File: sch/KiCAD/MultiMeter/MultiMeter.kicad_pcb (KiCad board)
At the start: 2 copper layers, 35.6 x 52.7 mm, 20 parts, among them J1 Conn_01x02_Male, J2 Conn_01x02_Male, J3 Conn_01x03_Male, J4 Conn_01x03_Male, J5 Conn_01x02_Female, J6 Conn_01x15, J7 Conn_01x15

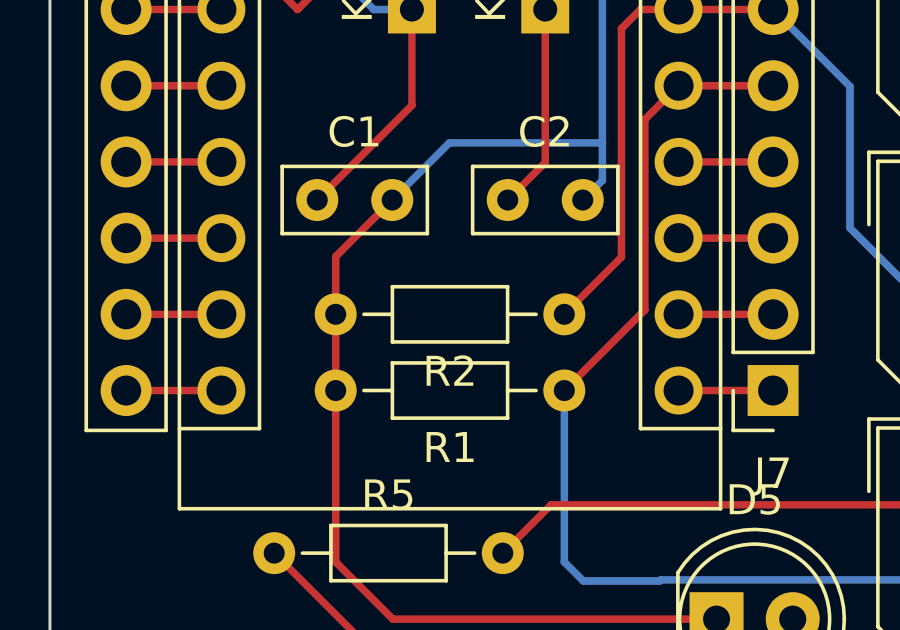
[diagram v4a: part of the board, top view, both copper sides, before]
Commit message: 回路図微修正
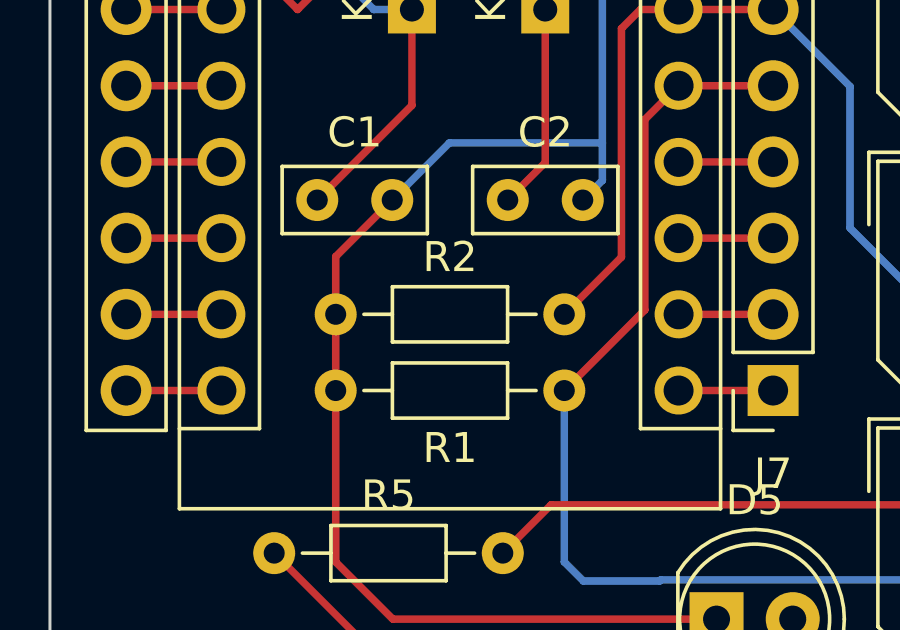
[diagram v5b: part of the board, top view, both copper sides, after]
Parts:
- C1, C2: value C -> 0.1uF
- R1, R2, R3, R4: value R -> 10K ohm
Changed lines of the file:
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@@
       (effects (font (size 1 1) (thickness 0.15)))
     )
-    (fp_text value "C" (at 1.25 2.25) (layer "F.Fab")
+    (fp_text value "0.1uF" (at 1.25 2.25) (layer "F.Fab")
       (effects (font (size 1 1) (thickness 0.15)))
     )
@@
       (effects (font (size 1 1) (thickness 0.15)))
     )
-    (fp_text value "C" (at 1.25 2.25) (layer "F.Fab")
+    (fp_text value "0.1uF" (at 1.25 2.25) (layer "F.Fab")
       (effects (font (size 1 1) (thickness 0.15)))
     )
@@
       (effects (font (size 1 1) (thickness 0.15)))
     )
-    (fp_text value "R" (at 3.81 1.92) (layer "F.Fab")
+    (fp_text value "10K ohm" (at 3.81 1.92) (layer "F.Fab")
       (effects (font (size 1 1) (thickness 0.15)))
     )
@@
     (property "Sheetname" "")
     (attr through_hole)
-    (fp_text reference "R2" (at 3.81 -1.92) (layer "F.SilkS")
-      (effects (font (size 1 1) (thickness 0.15)))
-    )
-    (fp_text value "R" (at 3.81 1.92) (layer "F.Fab")
+    (fp_text reference "R2" (at 3.81 1.905) (layer "F.SilkS")
+      (effects (font (size 1 1) (thickness 0.15)))
+    )
+    (fp_text value "10K ohm" (at 3.81 1.92) (layer "F.Fab")
       (effects (font (size 1 1) (thickness 0.15)))
     )
@@
       (effects (font (size 1 1) (thickness 0.15)))
     )
-    (fp_text value "R" (at 3.81 1.92) (layer "F.Fab")
+    (fp_text value "10K ohm" (at 3.81 1.92) (layer "F.Fab")
       (effects (font (size 1 1) (thickness 0.15)))
     )
@@
       (effects (font (size 1 1) (thickness 0.15)))
     )
-    (fp_text value "R" (at 3.81 1.92) (layer "F.Fab")
-      (effects (font (size 1 1) (thickness 0.15)))
-    )
+    (fp_text value "10K ohm" (at 3.81 1.92) (layer "F.Fab")
+      (effects (font (size 1 1) (thickness 0.15)))
+    )

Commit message: 基板修正
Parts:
- removed C1, C2: 0.1uF, Capacitor_THT:C_Rect_L4.6mm_W2.0mm_P2.50mm_MKS02_FKP02
- removed D1, D2, D3, D4: 1N4148, Diode_THT:D_DO-35_SOD27_P7.62mm_Horizontal
- added J8: Conn_01x08_Female, Connector_JST:JST_XH_B8B-XH-A_1x08_P2.50mm_Vertical, F.Cu at (40.3, 17.3)
- added JP1: Jumper_2_Open, Connector_PinHeader_2.54mm:PinHeader_1x02_P2.54mm_Vertical, F.Cu at (38.7, 67.3)
- added Q1: 2SC1815, Package_TO_SOT_THT:TO-92_Inline, F.Cu at (52.1, 34.6)
- added Q2: 2SC1815, Package_TO_SOT_THT:TO-92_Inline, F.Cu at (46.4, 34.6)
- added R10: 7K ohm, Resistor_THT:R_Axial_DIN0204_L3.6mm_D1.6mm_P7.62mm_Horizontal, F.Cu at (62.2, 19.7)
- added R11: 5K ohm, Resistor_THT:R_Axial_DIN0204_L3.6mm_D1.6mm_P7.62mm_Horizontal, F.Cu at (62.2, 22.9)
- added R6: 10K ohm, Resistor_THT:R_Axial_DIN0204_L3.6mm_D1.6mm_P7.62mm_Horizontal, F.Cu at (51.4, 39.4)
- added R7: 10K ohm, Resistor_THT:R_Axial_DIN0204_L3.6mm_D1.6mm_P7.62mm_Horizontal, F.Cu at (46.4, 39.4)
- added R8: 10K ohm, Resistor_THT:R_Axial_DIN0204_L3.6mm_D1.6mm_P7.62mm_Horizontal, F.Cu at (54.0, 47.0)
- added R9: 10K ohm, Resistor_THT:R_Axial_DIN0204_L3.6mm_D1.6mm_P7.62mm_Horizontal, F.Cu at (48.9, 47.0)
- added RV1: RV_Disc_D7mm_W4.5mm_P5mm, Varistor:RV_Disc_D7mm_W4.5mm_P5mm, F.Cu at (42.5, 67.3)
- added TP1: TestPoint, MountingHole:MountingHole_2.2mm_M2_DIN965_Pad, F.Cu at (64.8, 16.5)
- added TP2: TestPoint, MountingHole:MountingHole_2.2mm_M2_DIN965_Pad, F.Cu at (69.8, 16.5)
- J1, J2: footprint Connector_Molex:Molex_SPOX_5267-02A_1x02_P2.50mm_Vertical -> Connector_Molex:Molex_SPOX_5268-02A_1x02_P2.50mm_Horizontal
- J3, J4: footprint Connector_Molex:Molex_SPOX_5267-03A_1x03_P2.50mm_Vertical -> Connector_Molex:Molex_SPOX_5268-03A_1x03_P2.50mm_Horizontal
- moved R5 11.7 mm to (55.2, 71.1), turned to 90 degrees
- moved J4 5.17 mm to (65.2, 38.7), turned to 90 degrees
- moved J3 5.16 mm to (65.4, 50.2), turned to 90 degrees
- moved J2 2.71 mm to (65.4, 59.1), turned to 90 degrees
- moved J1 2.71 mm to (65.4, 67.9), turned to 90 degrees
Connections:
- net Net-(A1-Pad27) renamed +5V
- net Net-(A1-Pad29) renamed GNDPWR
- R3 pad 1: Net-(A1-Pad5) -> Net-(Q1-Pad2)
- R4 pad 1: Net-(A1-Pad6) -> Net-(Q2-Pad2)
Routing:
- net Net-(A1-Pad6): track 57.4 -> 14.1 mm
- net Net-(JP1-Pad1): track 0.00 -> 38.6 mm
- net +5V: track 76.7 -> 109.5 mm
- net Net-(A1-Pad24): track 3.15 -> 32.4 mm
- net Net-(A1-Pad23): track 15.4 -> 42.7 mm
- net Net-(A1-Pad5): track 45.9 -> 20.6 mm
- net GNDPWR: track 118.4 -> 140.5 mm
- net Net-(Q1-Pad2): track 0.00 -> 17.7 mm
- net Net-(Q2-Pad2): track 0.00 -> 12.5 mm
- net Net-(D5-Pad2): track 19.2 -> 7.13 mm
- net Net-(R10-Pad1): track 0.00 -> 7.40 mm
- net Net-(Q1-Pad3): track 0.00 -> 4.98 mm
- net Net-(Q2-Pad3): track 0.00 -> 4.72 mm
- net throttle(+12V - 0V): track 0.00 -> 3.20 mm
- net Net-(A1-Pad21): track 28.0 -> 25.1 mm
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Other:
- board size 35.6 x 52.7 mm -> 35.6 x 58.5 mm
- board text added: "2023/07/01"
- board text removed: "2022/09/13"

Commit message: 回路図修正
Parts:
- added J9: Conn_01x02_Female, Connector_Molex:Molex_KK-254_AE-6410-02A_1x02_P2.54mm_Vertical, F.Cu at (52.8, 69.1)
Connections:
- net Net-(A1-Pad30) renamed +12V
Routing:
- net +12V: track 3.15 -> 93.0 mm
- net GNDPWR: track 140.5 -> 141.4 mm

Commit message: 回路図修正
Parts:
- removed R10: 7K ohm, Resistor_THT:R_Axial_DIN0204_L3.6mm_D1.6mm_P7.62mm_Horizontal
- removed R11: 5K ohm, Resistor_THT:R_Axial_DIN0204_L3.6mm_D1.6mm_P7.62mm_Horizontal
- removed TP1, TP2: TestPoint, MountingHole:MountingHole_2.2mm_M2_DIN965_Pad
- J5: value Conn_01x02_Female -> Conn_01x03_Female; footprint Connector_Molex:Molex_KK-254_AE-6410-02A_1x02_P2.54mm_Vertical -> Connector_Molex:Molex_KK-254_AE-6410-03A_1x03_P2.54mm_Vertical
- moved RV1 56.2 mm to (64.3, 15.5), turned to -90 degrees
- moved J9 54.8 mm to (69.1, 16.8), turned to -90 degrees
- moved JP1 18.0 mm to (48.8, 52.3)
- moved J5 2.42 mm to (66.8, 23.6)
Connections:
- J4 pad 2: Net-(A1-Pad23) -> Net-(A1-Pad25)
- Q2 pad 3: Net-(Q2-Pad3) -> GNDPWR
- R9 pad 2: Net-(Q2-Pad3) -> GNDPWR
- RV1 pad 1: +5V -> +12V
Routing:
- net +12V: track 93.0 -> 20.3 mm
- net Net-(JP1-Pad1): track 38.6 -> 12.3 mm
- net Net-(A1-Pad26): track 3.15 -> 13.1 mm
- net +5V: track 109.5 -> 101.0 mm
- net Net-(A1-Pad23): track 42.7 -> 50.5 mm
- net Net-(R10-Pad1): track 7.40 -> 0.00 mm
- net Net-(A1-Pad25): track 3.15 -> 8.44 mm
- net Net-(Q2-Pad3): track 4.72 -> 0.00 mm
- net GNDPWR: track 141.4 -> 136.8 mm
- net throttle(+12V - 0V): track 3.20 -> 0.00 mm
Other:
- board text added: "Th Sp Tc"
- board text removed: "Sp Tc"
